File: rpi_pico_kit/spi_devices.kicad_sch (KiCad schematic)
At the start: 20 parts, among them J6 Conn_01x08_Male, J7 Conn_01x08_Male, J8 Conn_01x08_Male, J9 Micro_SD_Card_Det, SW10 SW_Push, SW7 SW_Push, SW8 SW_Push, SW9 SW_Push, U7 MCP23S08-xSO

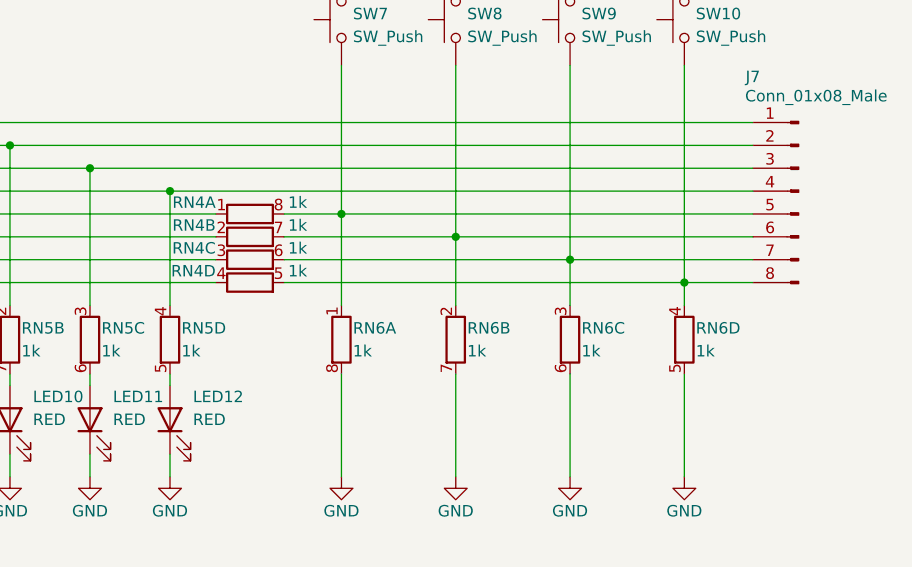
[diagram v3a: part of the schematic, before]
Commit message: spi (unrouted 319)
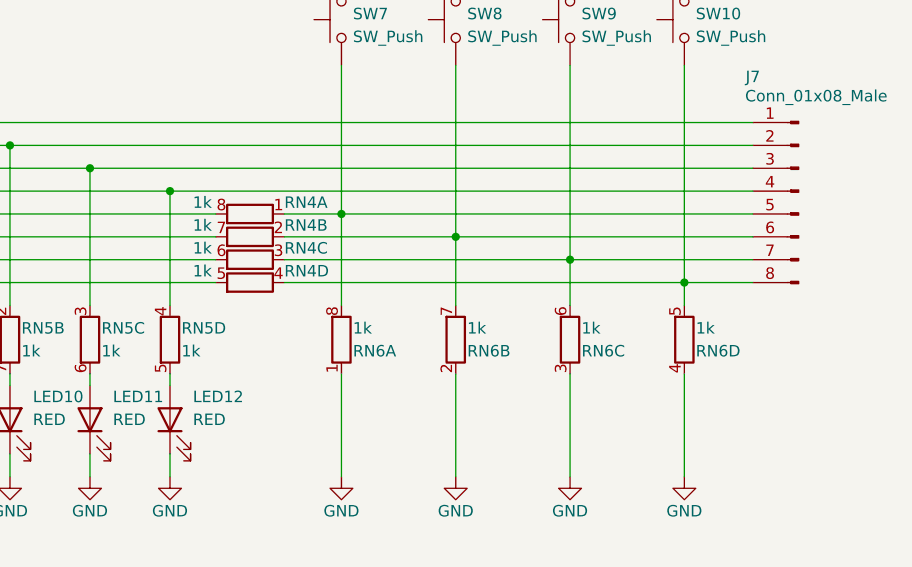
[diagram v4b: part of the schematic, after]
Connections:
- net GND: now also RN6.1 (R1.1), RN6.2 (R2.1), RN6.3 (R3.1), RN6.4 (R4.1); no longer RN6.5 (R4.2), RN6.6 (R3.2), RN6.7 (R2.2), RN6.8 (R1.2)
- net GP4: now also RN4.8 (R1.2); no longer RN4.1 (R1.1)
- net GP5: now also RN4.7 (R2.2); no longer RN4.2 (R2.1)
- net GP6: now also RN4.6 (R3.2); no longer RN4.3 (R3.1)
- net GP7: now also RN4.5 (R4.2); no longer RN4.4 (R4.1)
- net at J7.5 (Pin_5), SW7.1: now also RN4.1 (R1.1), RN6.8 (R1.2); no longer RN4.8 (R1.2), RN6.1 (R1.1)
- net at J7.7 (Pin_7), SW9.1: now also RN4.3 (R3.1), RN6.6 (R3.2); no longer RN4.6 (R3.2), RN6.3 (R3.1)
- net at J7.6 (Pin_6), SW8.1: now also RN4.2 (R2.1), RN6.7 (R2.2); no longer RN4.7 (R2.2), RN6.2 (R2.1)
- net at J7.8 (Pin_8), SW10.1: now also RN4.4 (R4.1), RN6.5 (R4.2); no longer RN4.5 (R4.2), RN6.4 (R4.1)
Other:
- moved on the sheet: RN4A, RN4B, RN4C, RN4D, RN6A, RN6B, RN6C, RN6D
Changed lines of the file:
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@@
     (pin "1")
   )
-  (symbol (lib_id "Device:R_Pack04_Split") (at 123.19 59.69 270) (unit 1)
-    (in_bom yes) (on_board yes)
-    (property "Reference" "RN4" (id 0) (at 119.38 58.42 90)
-      (effects (font (size 1.27 1.27)) (justify right))
-    )
-    (property "Value" "1k" (id 1) (at 129.54 58.42 90)
+  (symbol (lib_id "Device:R_Pack04_Split") (at 123.19 59.69 90) (mirror x) (unit 1)
+    (in_bom yes) (on_board yes)
+    (property "Reference" "RN4" (id 0) (at 127 58.42 90)
+      (effects (font (size 1.27 1.27)) (justify right))
+    )
+    (property "Value" "1k" (id 1) (at 116.84 58.42 90)
       (effects (font (size 1.27 1.27)) (justify right))
     )
@@
     (pin "1")
   )
-  (symbol (lib_id "Device:R_Pack04_Split") (at 133.35 73.66 180) (unit 1)
-    (in_bom yes) (on_board yes)
-    (property "Reference" "RN6" (id 0) (at 134.62 72.39 0)
-      (effects (font (size 1.27 1.27)) (justify right))
-    )
-    (property "Value" "1k" (id 1) (at 134.62 74.93 0)
+  (symbol (lib_id "Device:R_Pack04_Split") (at 133.35 73.66 0) (mirror y) (unit 1)
+    (in_bom yes) (on_board yes)
+    (property "Reference" "RN6" (id 0) (at 134.62 74.93 0)
+      (effects (font (size 1.27 1.27)) (justify right))
+    )
+    (property "Value" "1k" (id 1) (at 134.62 72.39 0)
       (effects (font (size 1.27 1.27)) (justify right))
     )
@@
     (pin "1")
   )
-  (symbol (lib_id "Device:R_Pack04_Split") (at 123.19 64.77 270) (unit 3)
-    (in_bom yes) (on_board yes)
-    (property "Reference" "RN4" (id 0) (at 119.38 63.5 90)
-      (effects (font (size 1.27 1.27)) (justify right))
-    )
-    (property "Value" "1k" (id 1) (at 129.54 63.5 90)
+  (symbol (lib_id "Device:R_Pack04_Split") (at 123.19 64.77 90) (mirror x) (unit 3)
+    (in_bom yes) (on_board yes)
+    (property "Reference" "RN4" (id 0) (at 127 63.5 90)
+      (effects (font (size 1.27 1.27)) (justify right))
+    )
+    (property "Value" "1k" (id 1) (at 116.84 63.5 90)
       (effects (font (size 1.27 1.27)) (justify right))
     )
@@
     (pin "1")
   )
-  (symbol (lib_id "Device:R_Pack04_Split") (at 171.45 73.66 180) (unit 4)
-    (in_bom yes) (on_board yes)
-    (property "Reference" "RN6" (id 0) (at 172.72 72.39 0)
-      (effects (font (size 1.27 1.27)) (justify right))
-    )
-    (property "Value" "1k" (id 1) (at 172.72 74.93 0)
+  (symbol (lib_id "Device:R_Pack04_Split") (at 171.45 73.66 0) (mirror y) (unit 4)
+    (in_bom yes) (on_board yes)
+    (property "Reference" "RN6" (id 0) (at 172.72 74.93 0)
+      (effects (font (size 1.27 1.27)) (justify right))
+    )
+    (property "Value" "1k" (id 1) (at 172.72 72.39 0)
       (effects (font (size 1.27 1.27)) (justify right))
     )
@@
     (pin "8")
   )
-  (symbol (lib_id "Device:R_Pack04_Split") (at 123.19 62.23 270) (unit 2)
-    (in_bom yes) (on_board yes)
-    (property "Reference" "RN4" (id 0) (at 119.38 60.96 90)
-      (effects (font (size 1.27 1.27)) (justify right))
-    )
-    (property "Value" "1k" (id 1) (at 129.54 60.96 90)
+  (symbol (lib_id "Device:R_Pack04_Split") (at 123.19 62.23 90) (mirror x) (unit 2)
+    (in_bom yes) (on_board yes)
+    (property "Reference" "RN4" (id 0) (at 127 60.96 90)
+      (effects (font (size 1.27 1.27)) (justify right))
+    )
+    (property "Value" "1k" (id 1) (at 116.84 60.96 90)
       (effects (font (size 1.27 1.27)) (justify right))
     )
@@
     (pin "1")
   )
-  (symbol (lib_id "Device:R_Pack04_Split") (at 146.05 73.66 180) (unit 2)
-    (in_bom yes) (on_board yes)
-    (property "Reference" "RN6" (id 0) (at 147.32 72.39 0)
-      (effects (font (size 1.27 1.27)) (justify right))
-    )
-    (property "Value" "1k" (id 1) (at 147.32 74.93 0)
+  (symbol (lib_id "Device:R_Pack04_Split") (at 146.05 73.66 0) (mirror y) (unit 2)
+    (in_bom yes) (on_board yes)
+    (property "Reference" "RN6" (id 0) (at 147.32 74.93 0)
+      (effects (font (size 1.27 1.27)) (justify right))
+    )
+    (property "Value" "1k" (id 1) (at 147.32 72.39 0)
       (effects (font (size 1.27 1.27)) (justify right))
     )
@@
     (pin "6")
   )
-  (symbol (lib_id "Device:R_Pack04_Split") (at 123.19 67.31 270) (unit 4)
-    (in_bom yes) (on_board yes)
-    (property "Reference" "RN4" (id 0) (at 119.38 66.04 90)
-      (effects (font (size 1.27 1.27)) (justify right))
-    )
-    (property "Value" "1k" (id 1) (at 129.54 66.04 90)
+  (symbol (lib_id "Device:R_Pack04_Split") (at 123.19 67.31 90) (mirror x) (unit 4)
+    (in_bom yes) (on_board yes)
+    (property "Reference" "RN4" (id 0) (at 127 66.04 90)
+      (effects (font (size 1.27 1.27)) (justify right))
+    )
+    (property "Value" "1k" (id 1) (at 116.84 66.04 90)
       (effects (font (size 1.27 1.27)) (justify right))
     )
@@
     (pin "2")
   )
-  (symbol (lib_id "Device:R_Pack04_Split") (at 158.75 73.66 180) (unit 3)
-    (in_bom yes) (on_board yes)
-    (property "Reference" "RN6" (id 0) (at 160.02 72.39 0)
-      (effects (font (size 1.27 1.27)) (justify right))
-    )
-    (property "Value" "1k" (id 1) (at 160.02 74.93 0)
-      (effects (font (size 1.27 1.27)) (justify right))
-    )
+  (symbol (lib_id "Device:R_Pack04_Split") (at 158.75 73.66 0) (mirror y) (unit 3)
+    (in_bom yes) (on_board yes)
+    (property "Reference" "RN6" (id 0) (at 160.02 74.93 0)
+      (effects (font (size 1.27 1.27)) (justify right))
+    )
+    (property "Value" "1k" (id 1) (at 160.02 72.39 0)
+      (effects (font (size 1.27 1.27)) (justify right))
+    )

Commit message: sd card (unrouted 92)
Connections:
- net MISO: now also RN7.1 (R1.1); no longer RN7.7 (R2.2)
- net MOSI: now also RN7.3 (R3.1); no longer RN7.6 (R3.2)
- net SCK: now also RN7.2 (R2.1); no longer RN7.8 (R1.2)
- net SD_CS: now also RN7.4 (R4.1); no longer RN7.5 (R4.2)
- net SPI_MISO: now also RN7.8 (R1.2); no longer RN7.2 (R2.1)
- net SPI_MOSI: now also RN7.6 (R3.2); no longer RN7.3 (R3.1)
- net SPI_SCK: now also RN7.7 (R2.2); no longer RN7.1 (R1.1)
- net SPI_SD_CS: now also RN7.5 (R4.2); no longer RN7.4 (R4.1)
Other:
- moved on the sheet: RN7A, RN7B, RN7C, RN7D
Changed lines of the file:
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@@
     (pin "8")
   )
-  (symbol (lib_id "Device:R_Pack04_Split") (at 111.76 125.73 270) (unit 1)
+  (symbol (lib_id "Device:R_Pack04_Split") (at 111.76 125.73 90) (mirror x) (unit 2)
     (in_bom yes) (on_board yes)
     (property "Reference" "RN7" (id 0) (at 111.76 123.19 90)
       (effects (font (size 1.27 1.27)) (justify right))
     )
-    (property "Value" "1k" (id 1) (at 115.57 123.19 90)
+    (property "Value" "1k" (id 1) (at 107.95 123.19 90)
       (effects (font (size 1.27 1.27)) (justify right))
     )
@@
       (effects (font (size 1.27 1.27)) hide)
     )
-    (pin "1")
-    (pin "8")
+    (pin "2")
+    (pin "7")
   )
   (symbol (lib_id "power:GND") (at 209.55 153.67 0) (unit 1)
@@
     (pin "1")
   )
-  (symbol (lib_id "Device:R_Pack04_Split") (at 111.76 130.81 270) (unit 2)
+  (symbol (lib_id "Device:R_Pack04_Split") (at 111.76 130.81 90) (mirror x) (unit 1)
     (in_bom yes) (on_board yes)
     (property "Reference" "RN7" (id 0) (at 111.76 128.27 90)
       (effects (font (size 1.27 1.27)) (justify right))
     )
-    (property "Value" "1k" (id 1) (at 115.57 128.27 90)
+    (property "Value" "1k" (id 1) (at 107.95 128.27 90)
       (effects (font (size 1.27 1.27)) (justify right))
     )
@@
       (effects (font (size 1.27 1.27)) hide)
     )
-    (pin "2")
-    (pin "7")
+    (pin "1")
+    (pin "8")
   )
   (symbol (lib_name "MCP23S08-xSO_1") (lib_id "Interface_Expansion:MCP23S08-xSO") (at 62.23 59.69 0) (unit 1)
@@
     (pin "7")
   )
-  (symbol (lib_id "Device:R_Pack04_Split") (at 111.76 140.97 270) (unit 4)
+  (symbol (lib_id "Device:R_Pack04_Split") (at 111.76 140.97 90) (mirror x) (unit 4)
     (in_bom yes) (on_board yes)
     (property "Reference" "RN7" (id 0) (at 111.76 138.43 90)
       (effects (font (size 1.27 1.27)) (justify right))
     )
-    (property "Value" "1k" (id 1) (at 115.57 138.43 90)
+    (property "Value" "1k" (id 1) (at 107.95 138.43 90)
       (effects (font (size 1.27 1.27)) (justify right))
     )
@@
     (pin "1")
   )
-  (symbol (lib_id "Device:R_Pack04_Split") (at 111.76 135.89 270) (unit 3)
+  (symbol (lib_id "Device:R_Pack04_Split") (at 111.76 135.89 90) (mirror x) (unit 3)
     (in_bom yes) (on_board yes)
     (property "Reference" "RN7" (id 0) (at 111.76 133.35 90)
       (effects (font (size 1.27 1.27)) (justify right))
     )
-    (property "Value" "1k" (id 1) (at 115.57 133.35 90)
-      (effects (font (size 1.27 1.27)) (justify right))
-    )
+    (property "Value" "1k" (id 1) (at 107.95 133.35 90)
+      (effects (font (size 1.27 1.27)) (justify right))
+    )

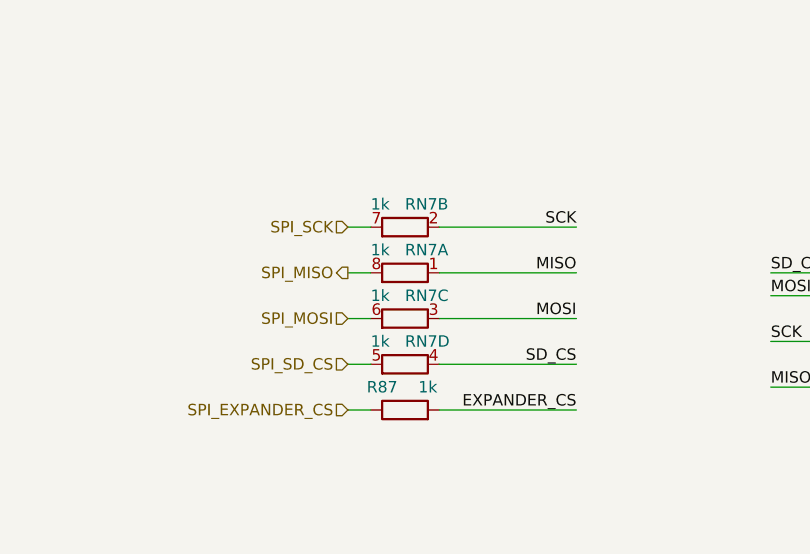
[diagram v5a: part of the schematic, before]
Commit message: sd card (unrouted 87)
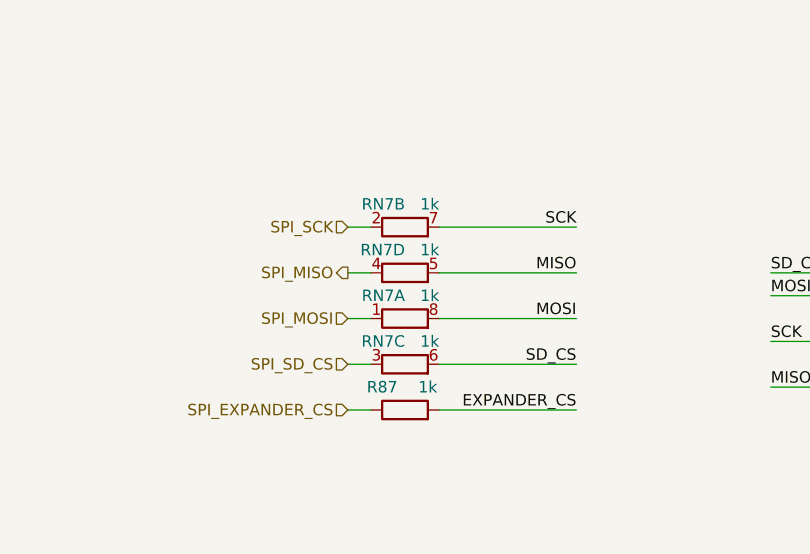
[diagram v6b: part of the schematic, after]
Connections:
- net MISO: now also RN7.5 (R4.2); no longer RN7.1 (R1.1)
- net MOSI: now also RN7.8 (R1.2); no longer RN7.3 (R3.1)
- net SCK: now also RN7.7 (R2.2); no longer RN7.2 (R2.1)
- net SD_CS: now also RN7.6 (R3.2); no longer RN7.4 (R4.1)
- net SPI_MISO: now also RN7.4 (R4.1); no longer RN7.8 (R1.2)
- net SPI_MOSI: now also RN7.1 (R1.1); no longer RN7.6 (R3.2)
- net SPI_SCK: now also RN7.2 (R2.1); no longer RN7.7 (R2.2)
- net SPI_SD_CS: now also RN7.3 (R3.1); no longer RN7.5 (R4.2)
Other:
- moved on the sheet: RN7A, RN7B, RN7C, RN7D
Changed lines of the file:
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@@
     (pin "8")
   )
-  (symbol (lib_id "Device:R_Pack04_Split") (at 111.76 125.73 90) (mirror x) (unit 2)
+  (symbol (lib_id "Device:R_Pack04_Split") (at 111.76 125.73 270) (unit 2)
     (in_bom yes) (on_board yes)
     (property "Reference" "RN7" (id 0) (at 111.76 123.19 90)
       (effects (font (size 1.27 1.27)) (justify right))
     )
-    (property "Value" "1k" (id 1) (at 107.95 123.19 90)
+    (property "Value" "1k" (id 1) (at 115.57 123.19 90)
       (effects (font (size 1.27 1.27)) (justify right))
     )
@@
     (pin "1")
   )
-  (symbol (lib_id "Device:R_Pack04_Split") (at 111.76 130.81 90) (mirror x) (unit 1)
+  (symbol (lib_id "Device:R_Pack04_Split") (at 111.76 130.81 270) (unit 4)
     (in_bom yes) (on_board yes)
     (property "Reference" "RN7" (id 0) (at 111.76 128.27 90)
       (effects (font (size 1.27 1.27)) (justify right))
     )
-    (property "Value" "1k" (id 1) (at 107.95 128.27 90)
+    (property "Value" "1k" (id 1) (at 115.57 128.27 90)
       (effects (font (size 1.27 1.27)) (justify right))
     )
@@
       (effects (font (size 1.27 1.27)) hide)
     )
-    (pin "1")
-    (pin "8")
+    (pin "4")
+    (pin "5")
   )
   (symbol (lib_name "MCP23S08-xSO_1") (lib_id "Interface_Expansion:MCP23S08-xSO") (at 62.23 59.69 0) (unit 1)
@@
     (pin "7")
   )
-  (symbol (lib_id "Device:R_Pack04_Split") (at 111.76 140.97 90) (mirror x) (unit 4)
+  (symbol (lib_id "Device:R_Pack04_Split") (at 111.76 140.97 270) (unit 3)
     (in_bom yes) (on_board yes)
     (property "Reference" "RN7" (id 0) (at 111.76 138.43 90)
       (effects (font (size 1.27 1.27)) (justify right))
     )
-    (property "Value" "1k" (id 1) (at 107.95 138.43 90)
+    (property "Value" "1k" (id 1) (at 115.57 138.43 90)
       (effects (font (size 1.27 1.27)) (justify right))
     )
@@
       (effects (font (size 1.27 1.27)) hide)
     )
-    (pin "4")
-    (pin "5")
+    (pin "3")
+    (pin "6")
   )
   (symbol (lib_id "power:GND") (at 158.75 88.9 0) (unit 1)
@@
     (pin "1")
   )
-  (symbol (lib_id "Device:R_Pack04_Split") (at 111.76 135.89 90) (mirror x) (unit 3)
+  (symbol (lib_id "Device:R_Pack04_Split") (at 111.76 135.89 270) (unit 1)
     (in_bom yes) (on_board yes)
     (property "Reference" "RN7" (id 0) (at 111.76 133.35 90)
       (effects (font (size 1.27 1.27)) (justify right))
     )
-    (property "Value" "1k" (id 1) (at 107.95 133.35 90)
+    (property "Value" "1k" (id 1) (at 115.57 133.35 90)
       (effects (font (size 1.27 1.27)) (justify right))
     )
@@
       (effects (font (size 1.27 1.27)) hide)
     )
-    (pin "3")
-    (pin "6")
+    (pin "1")
+    (pin "8")
   )
   (symbol (lib_id "Device:R_Pack04_Split") (at 123.19 67.31 90) (mirror x) (unit 4)
